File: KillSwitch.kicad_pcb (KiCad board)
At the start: 2 copper layers, 64 x 29.5 mm, 26 parts, among them J0 Screw_Terminal_1x04, J3 CONN_01X02, Q0 IRF1324PBF, Q1 IRF1324PBF, Q2 IRF1324PBF, Q3 IRF1324PBF, U0 NC7SZ08, U1 TPS62175, U2 4013

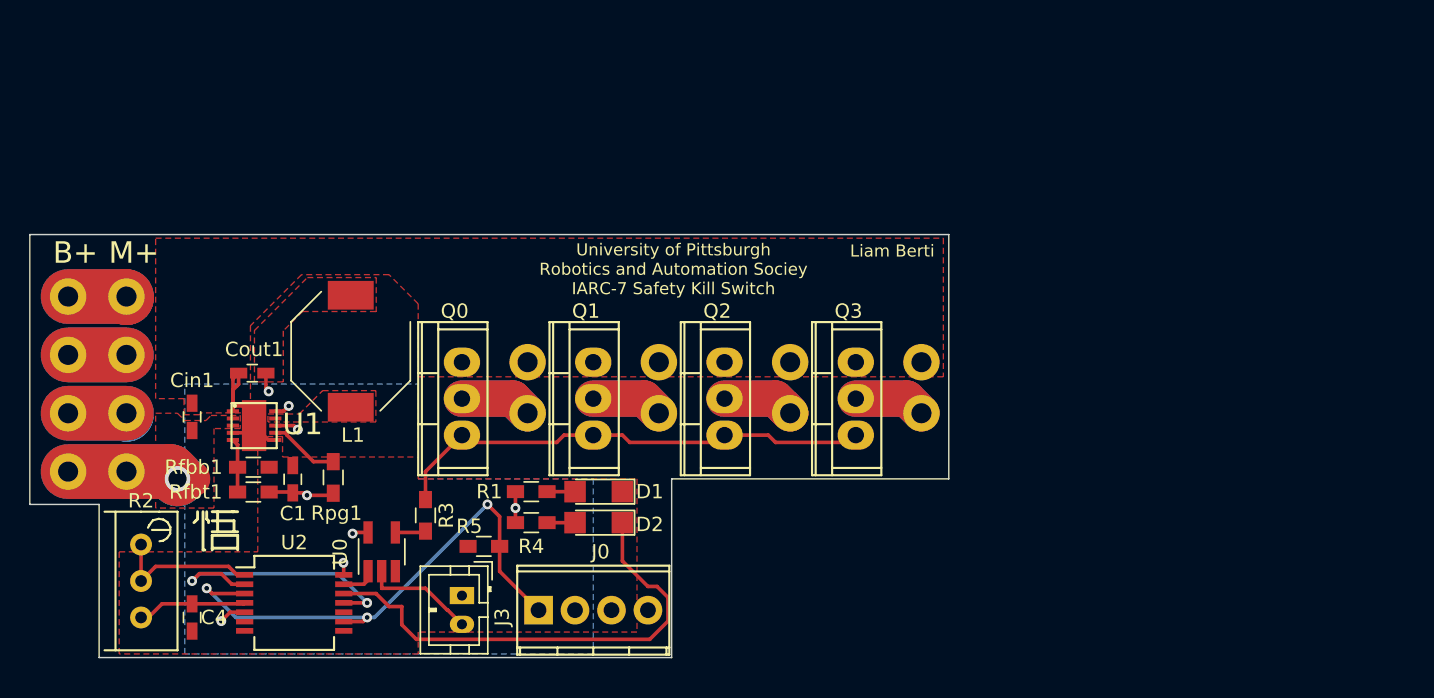
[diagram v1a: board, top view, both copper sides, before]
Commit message: Added standoff holes to pcb
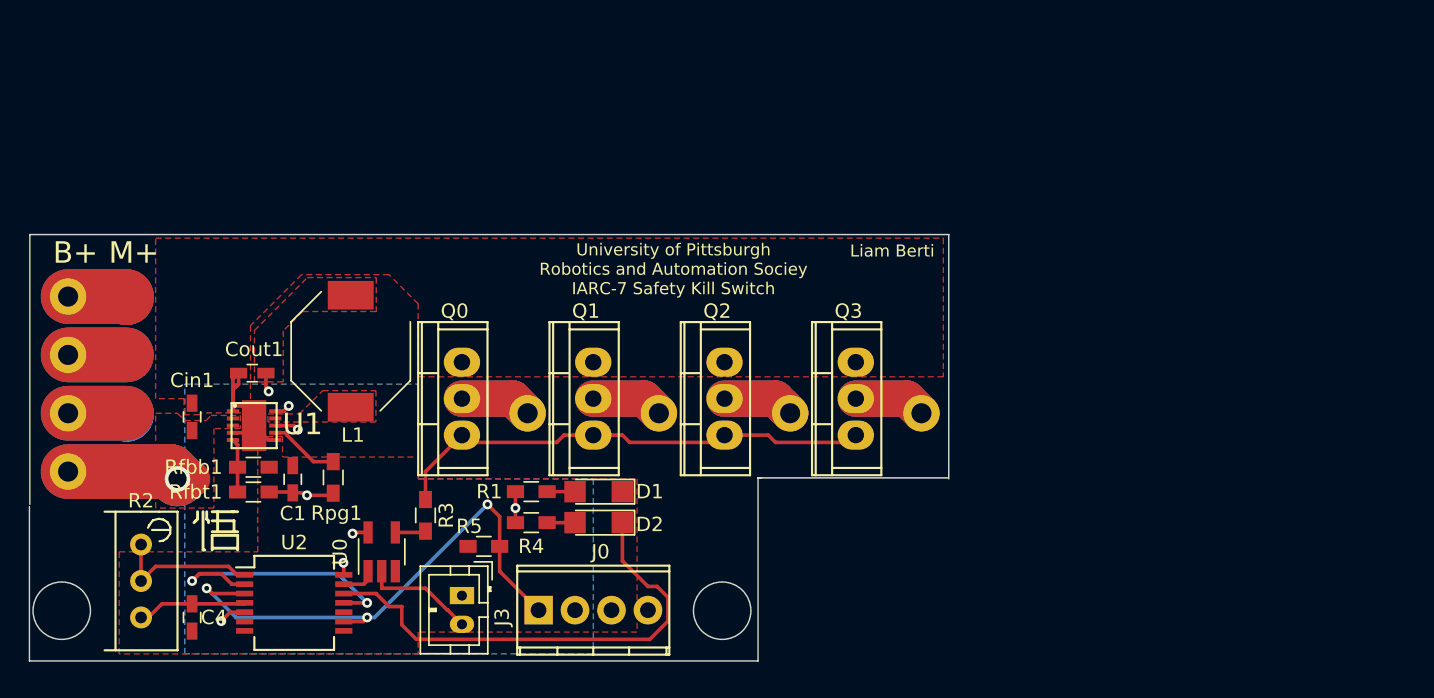
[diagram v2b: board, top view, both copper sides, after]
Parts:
- removed the ? at (157.9, 72.6)
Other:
- board size 64 x 29.5 mm -> 64 x 29.7 mm
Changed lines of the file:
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@@
 (kicad_pcb (version 4) (host pcbnew 4.0.6)
   (general
-    (links 69)
+    (links 61)
     (no_connects 0)
-    (area 120.726999 66.751999 184.835001 96.316001)
+    (area 120.726999 56.4592 210.820001 156.290001)
     (thickness 0.8128)
-    (drawings 31)
+    (drawings 35)
     (tracks 183)
     (zones 0)
-    (modules 26)
+    (modules 25)
     (nets 27)
   )
@@
   )
   (module Wire_Pads:barrel_connector (layer Top)
-    (at 157.861 72.644 180)
-    (fp_text reference "" (at -0.9525 11.176 180) (layer F.SilkS)
-      (effects (font (size 1 1) (thickness 0.15)))
-    )
-    (fp_text value CONN_01X08 (at 0 -0.5 180) (layer F.Fab)
-      (effects (font (size 1 1) (thickness 0.15)))
-    )
-    (pad 1 thru_hole circle (at -15.875 -3.048 180) (size 2.54 2.54) (drill 1.397) (layers *.Cu *.Mask)
-      (net 2 Earth))
-    (pad 2 thru_hole circle (at -25.019 -3.048 180) (size 2.54 2.54) (drill 1.397) (layers *.Cu *.Mask)
-      (net 2 Earth))
-    (pad 3 thru_hole circle (at -6.731 -3.048 180) (size 2.54 2.54) (drill 1.397) (layers *.Cu *.Mask)
-      (net 2 Earth))
-    (pad 4 thru_hole circle (at 2.413 -3.048 180) (size 2.54 2.54) (drill 1.397) (layers *.Cu *.Mask)
-      (net 2 Earth))
-    (pad 5 thru_hole circle (at 30.353 -10.668 180) (size 2.54 2.54) (drill 1.397) (layers *.Cu *.Mask)
-      (net 4 /VbattPos))
-    (pad 6 thru_hole circle (at 30.353 -6.604 180) (size 2.54 2.54) (drill 1.397) (layers *.Cu *.Mask)
-      (net 17 "Net-(J1-Pad6)"))
-    (pad 7 thru_hole circle (at 30.353 -2.54 180) (size 2.54 2.54) (drill 1.397) (layers *.Cu *.Mask)
-      (net 18 "Net-(J1-Pad7)"))
-    (pad 8 thru_hole circle (at 30.353 1.524 180) (size 2.54 2.54) (drill 1.397) (layers *.Cu *.Mask)
-      (net 19 "Net-(J1-Pad8)"))
-  )
-  (module Wire_Pads:barrel_connector (layer Top)
     (at 169.164 57.912)
     (fp_text reference "" (at 0 0.5) (layer F.SilkS)
@@
     )
   )
+  (dimension 4 (width 0.3) (layer Eco1.User)
+    (gr_text "4.000 mm" (at 175.35 93 90) (layer Eco1.User)
+      (effects (font (size 1.5 1.5) (thickness 0.3)))
+    )
+    (feature1 (pts (xy 169 91) (xy 176.7 91)))
+    (feature2 (pts (xy 169 95) (xy 176.7 95)))
+    (crossbar (pts (xy 174 95) (xy 174 91)))
+    (arrow1a (pts (xy 174 91) (xy 174.586421 92.126504)))
+    (arrow1b (pts (xy 174 91) (xy 173.413579 92.126504)))
+    (arrow2a (pts (xy 174 95) (xy 174.586421 93.873496)))
+    (arrow2b (pts (xy 174 95) (xy 173.413579 93.873496)))
+  )
+  (dimension 4 (width 0.3) (layer Eco1.User)
+    (gr_text "4.000 mm" (at 115.65 93 90) (layer Eco1.User)
+      (effects (font (size 1.5 1.5) (thickness 0.3)))
+    )
+    (feature1 (pts (xy 123 91) (xy 114.3 91)))
+    (feature2 (pts (xy 123 95) (xy 114.3 95)))
+    (crossbar (pts (xy 117 95) (xy 117 91)))
+    (arrow1a (pts (xy 117 91) (xy 117.586421 92.126504)))
+    (arrow1b (pts (xy 117 91) (xy 116.413579 92.126504)))
+    (arrow2a (pts (xy 117 95) (xy 117.586421 93.873496)))
+    (arrow2b (pts (xy 117 95) (xy 116.413579 93.873496)))
+  )
+  (dimension 46 (width 0.3) (layer Eco1.User)
+    (gr_text "46.000 mm" (at 146 100.35) (layer Eco1.User)
+      (effects (font (size 1.5 1.5) (thickness 0.3)))
+    )
+    (feature1 (pts (xy 123 93) (xy 123 101.7)))
+    (feature2 (pts (xy 169 93) (xy 169 101.7)))
+    (crossbar (pts (xy 169 99) (xy 123 99)))
+    (arrow1a (pts (xy 123 99) (xy 124.126504 98.413579)))
+    (arrow1b (pts (xy 123 99) (xy 124.126504 99.586421)))
+    (arrow2a (pts (xy 169 99) (xy 167.873496 98.413579)))
+    (arrow2b (pts (xy 169 99) (xy 167.873496 99.586421)))
+  )
+  (gr_line (start 171.5 83.75) (end 184.75 83.75) (angle 90) (layer Edge.Cuts) (width 0.1))
+  (gr_line (start 171.5 83.75) (end 171.75 83.75) (angle 90) (layer Edge.Cuts) (width 0.1))
+  (gr_line (start 171.5 96.5) (end 171.5 83.75) (angle 90) (layer Edge.Cuts) (width 0.1))
+  (gr_line (start 120.75 96.5) (end 171.5 96.5) (angle 90) (layer Edge.Cuts) (width 0.1))
+  (gr_line (start 120.75 85.75) (end 120.75 96.5) (angle 90) (layer Edge.Cuts) (width 0.1))
+  (gr_circle (center 123 93) (end 123 91) (layer Edge.Cuts) (width 0.1))
+  (gr_circle (center 169 93) (end 169 91) (layer Edge.Cuts) (width 0.1))
   (gr_line (start 133.477 88.646) (end 135.255 88.646) (angle 90) (layer F.SilkS) (width 0.2))
   (gr_line (start 135.255 87.757) (end 135.255 88.773) (angle 90) (layer F.SilkS) (width 0.2))
@@
     (effects (font (size 0.8396 0.8396) (thickness 0.2099)))
   )
-  (gr_line (start 125.603 85.598) (end 120.777 85.598) (angle 90) (layer Edge.Cuts) (width 0.1))
-  (gr_line (start 125.603 96.266) (end 125.603 85.598) (angle 90) (layer Edge.Cuts) (width 0.1))
-  (gr_line (start 165.481 96.266) (end 125.603 96.266) (angle 90) (layer Edge.Cuts) (width 0.1))
-  (gr_line (start 165.481 83.82) (end 165.481 96.266) (angle 90) (layer Edge.Cuts) (width 0.1))
-  (gr_line (start 184.785 83.82) (end 165.481 83.82) (angle 90) (layer Edge.Cuts) (width 0.1))
   (gr_line (start 184.785 66.802) (end 184.785 83.82) (angle 90) (layer Edge.Cuts) (width 0.1))
   (gr_line (start 120.777 66.802) (end 184.785 66.802) (angle 90) (layer Edge.Cuts) (width 0.1))
@@
     (effects (font (size 1.5 1.5) (thickness 0.3)))
   )
-  (dimension 50.8 (width 0.3) (layer Eco2.User)
-    (gr_text "2.0000 in" (at 185.42 154.94) (layer Eco2.User)
-      (effects (font (size 1.5 1.5) (thickness 0.3)))
-    )
-    (feature1 (pts (xy 160.02 154.94) (xy 160.02 154.94)))
-    (feature2 (pts (xy 210.82 154.94) (xy 210.82 154.94)))
-    (crossbar (pts (xy 210.82 154.94) (xy 160.02 154.94)))
-    (arrow1a (pts (xy 160.02 154.94) (xy 161.146504 154.353579)))
-    (arrow1b (pts (xy 160.02 154.94) (xy 161.146504 155.526421)))
-    (arrow2a (pts (xy 210.82 154.94) (xy 209.693496 154.353579)))
-    (arrow2b (pts (xy 210.82 154.94) (xy 209.693496 155.526421)))
-  )
   (segment (start 140.081 84.963) (end 141.7652 84.963) (width 0.254) (layer Top) (net 1))

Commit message: Added standoff holes to pcb FIX
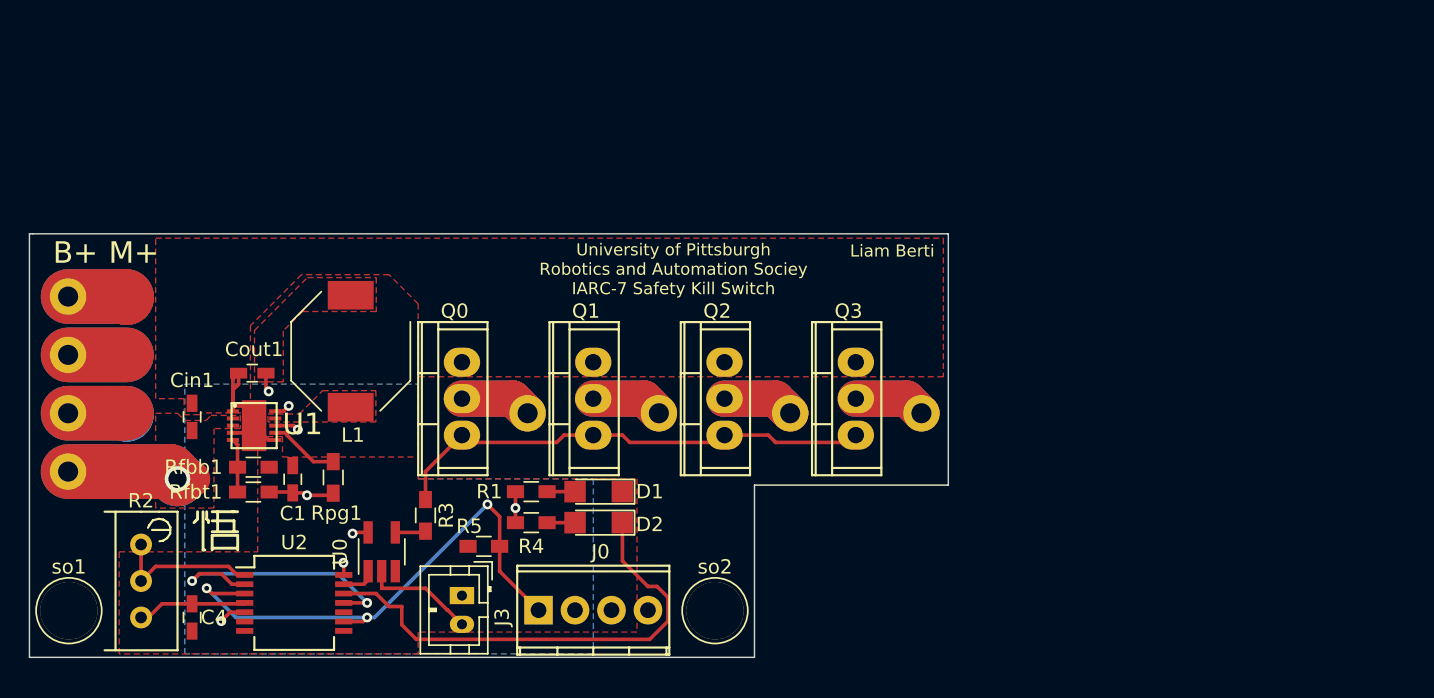
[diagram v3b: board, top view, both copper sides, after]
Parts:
- added so1: 1pin, UserParts:4mmhole, F.Cu at (123.5, 93.0)
- added so2: 1pin, UserParts:4mmhole, F.Cu at (168.5, 93.0)
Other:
- board size 64 x 29.7 mm -> 64 x 29.5 mm
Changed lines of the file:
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@@
     (links 61)
     (no_connects 0)
-    (area 120.726999 56.4592 210.820001 156.290001)
+    (area 120.699999 66.751999 184.835001 96.550001)
     (thickness 0.8128)
-    (drawings 35)
+    (drawings 32)
     (tracks 183)
     (zones 0)
-    (modules 25)
+    (modules 27)
     (nets 27)
   )
@@
     )
   )
+  (module UserParts:4mmhole (layer Top)
+    (at 123.5 93)
+    (descr "module 1 pin (ou trou mecanique de percage)")
+    (tags DEV)
+    (fp_text reference so1 (at 0 -3.048) (layer F.SilkS)
+      (effects (font (size 1 1) (thickness 0.15)))
+    )
+    (fp_text value 1pin (at 0 3) (layer F.Fab)
+      (effects (font (size 1 1) (thickness 0.15)))
+    )
+    (fp_circle (center 0 0) (end 2 0.8) (layer F.Fab) (width 0.1))
+    (fp_circle (center 0 0) (end 2.6 0) (layer F.CrtYd) (width 0.05))
+    (fp_circle (center 0 0) (end 0 -2.286) (layer F.SilkS) (width 0.12))
+    (pad 1 thru_hole circle (at 0 0) (size 4 4) (drill 4) (layers *.Cu *.Mask))
+  )
+  (module UserParts:4mmhole (layer Top)
+    (at 168.5 93)
+    (descr "module 1 pin (ou trou mecanique de percage)")
+    (tags DEV)
+    (fp_text reference so2 (at 0 -3.048) (layer F.SilkS)
+      (effects (font (size 1 1) (thickness 0.15)))
+    )
+    (fp_text value 1pin (at 0 3) (layer F.Fab)
+      (effects (font (size 1 1) (thickness 0.15)))
+    )
+    (fp_circle (center 0 0) (end 2 0.8) (layer F.Fab) (width 0.1))
+    (fp_circle (center 0 0) (end 2.6 0) (layer F.CrtYd) (width 0.05))
+    (fp_circle (center 0 0) (end 0 -2.286) (layer F.SilkS) (width 0.12))
+    (pad 1 thru_hole circle (at 0 0) (size 4 4) (drill 4) (layers *.Cu *.Mask))
+  )
+  (gr_line (start 120.75 66.75) (end 120.75 96.25) (angle 90) (layer Edge.Cuts) (width 0.1))
+  (gr_line (start 121 66.75) (end 120.75 66.75) (angle 90) (layer Edge.Cuts) (width 0.1))
+  (gr_line (start 184.75 66.75) (end 121 66.75) (angle 90) (layer Edge.Cuts) (width 0.1))
+  (gr_line (start 184.75 84.25) (end 184.75 66.75) (angle 90) (layer Edge.Cuts) (width 0.1))
+  (gr_line (start 171.25 84.25) (end 184.75 84.25) (angle 90) (layer Edge.Cuts) (width 0.1))
+  (gr_line (start 171.25 96.25) (end 171.25 84.25) (angle 90) (layer Edge.Cuts) (width 0.1))
+  (gr_line (start 120.75 96.25) (end 171.25 96.25) (angle 90) (layer Edge.Cuts) (width 0.1))
+  (dimension 45 (width 0.3) (layer Eco1.User)
+    (gr_text "45.000 mm" (at 146 100.85) (layer Eco1.User)
+      (effects (font (size 1.5 1.5) (thickness 0.3)))
+    )
+    (feature1 (pts (xy 123.5 93) (xy 123.5 102.2)))
+    (feature2 (pts (xy 168.5 93) (xy 168.5 102.2)))
+    (crossbar (pts (xy 168.5 99.5) (xy 123.5 99.5)))
+    (arrow1a (pts (xy 123.5 99.5) (xy 124.626504 98.913579)))
+    (arrow1b (pts (xy 123.5 99.5) (xy 124.626504 100.086421)))
+    (arrow2a (pts (xy 168.5 99.5) (xy 167.373496 98.913579)))
+    (arrow2b (pts (xy 168.5 99.5) (xy 167.373496 100.086421)))
+  )
   (dimension 4 (width 0.3) (layer Eco1.User)
     (gr_text "4.000 mm" (at 175.35 93 90) (layer Eco1.User)
@@
     (arrow2b (pts (xy 117 95) (xy 116.413579 93.873496)))
   )
-  (dimension 46 (width 0.3) (layer Eco1.User)
-    (gr_text "46.000 mm" (at 146 100.35) (layer Eco1.User)
-      (effects (font (size 1.5 1.5) (thickness 0.3)))
-    )
-    (feature1 (pts (xy 123 93) (xy 123 101.7)))
-    (feature2 (pts (xy 169 93) (xy 169 101.7)))
-    (crossbar (pts (xy 169 99) (xy 123 99)))
-    (arrow1a (pts (xy 123 99) (xy 124.126504 98.413579)))
-    (arrow1b (pts (xy 123 99) (xy 124.126504 99.586421)))
-    (arrow2a (pts (xy 169 99) (xy 167.873496 98.413579)))
-    (arrow2b (pts (xy 169 99) (xy 167.873496 99.586421)))
-  )
-  (gr_line (start 171.5 83.75) (end 184.75 83.75) (angle 90) (layer Edge.Cuts) (width 0.1))
-  (gr_line (start 171.5 83.75) (end 171.75 83.75) (angle 90) (layer Edge.Cuts) (width 0.1))
-  (gr_line (start 171.5 96.5) (end 171.5 83.75) (angle 90) (layer Edge.Cuts) (width 0.1))
-  (gr_line (start 120.75 96.5) (end 171.5 96.5) (angle 90) (layer Edge.Cuts) (width 0.1))
-  (gr_line (start 120.75 85.75) (end 120.75 96.5) (angle 90) (layer Edge.Cuts) (width 0.1))
-  (gr_circle (center 123 93) (end 123 91) (layer Edge.Cuts) (width 0.1))
-  (gr_circle (center 169 93) (end 169 91) (layer Edge.Cuts) (width 0.1))
   (gr_line (start 133.477 88.646) (end 135.255 88.646) (angle 90) (layer F.SilkS) (width 0.2))
   (gr_line (start 135.255 87.757) (end 135.255 88.773) (angle 90) (layer F.SilkS) (width 0.2))
@@
     (effects (font (size 0.8396 0.8396) (thickness 0.2099)))
   )
-  (gr_line (start 184.785 66.802) (end 184.785 83.82) (angle 90) (layer Edge.Cuts) (width 0.1))
-  (gr_line (start 120.777 66.802) (end 184.785 66.802) (angle 90) (layer Edge.Cuts) (width 0.1))
-  (gr_line (start 120.777 85.598) (end 120.777 66.802) (angle 90) (layer Edge.Cuts) (width 0.1))
   (gr_text "M+\n" (at 128.016 68.072) (layer F.SilkS)
     (effects (font (size 1.5 1.5) (thickness 0.3)))
